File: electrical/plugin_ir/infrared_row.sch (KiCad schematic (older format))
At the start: 17 parts, among them U2 QRE1113GR, U3 QRE1113GR, U4 QRE1113GR, U5 QRE1113GR, U6 QRE1113GR, U7 QRE1113GR, U8 QRE1113GR, U9 CD4051B

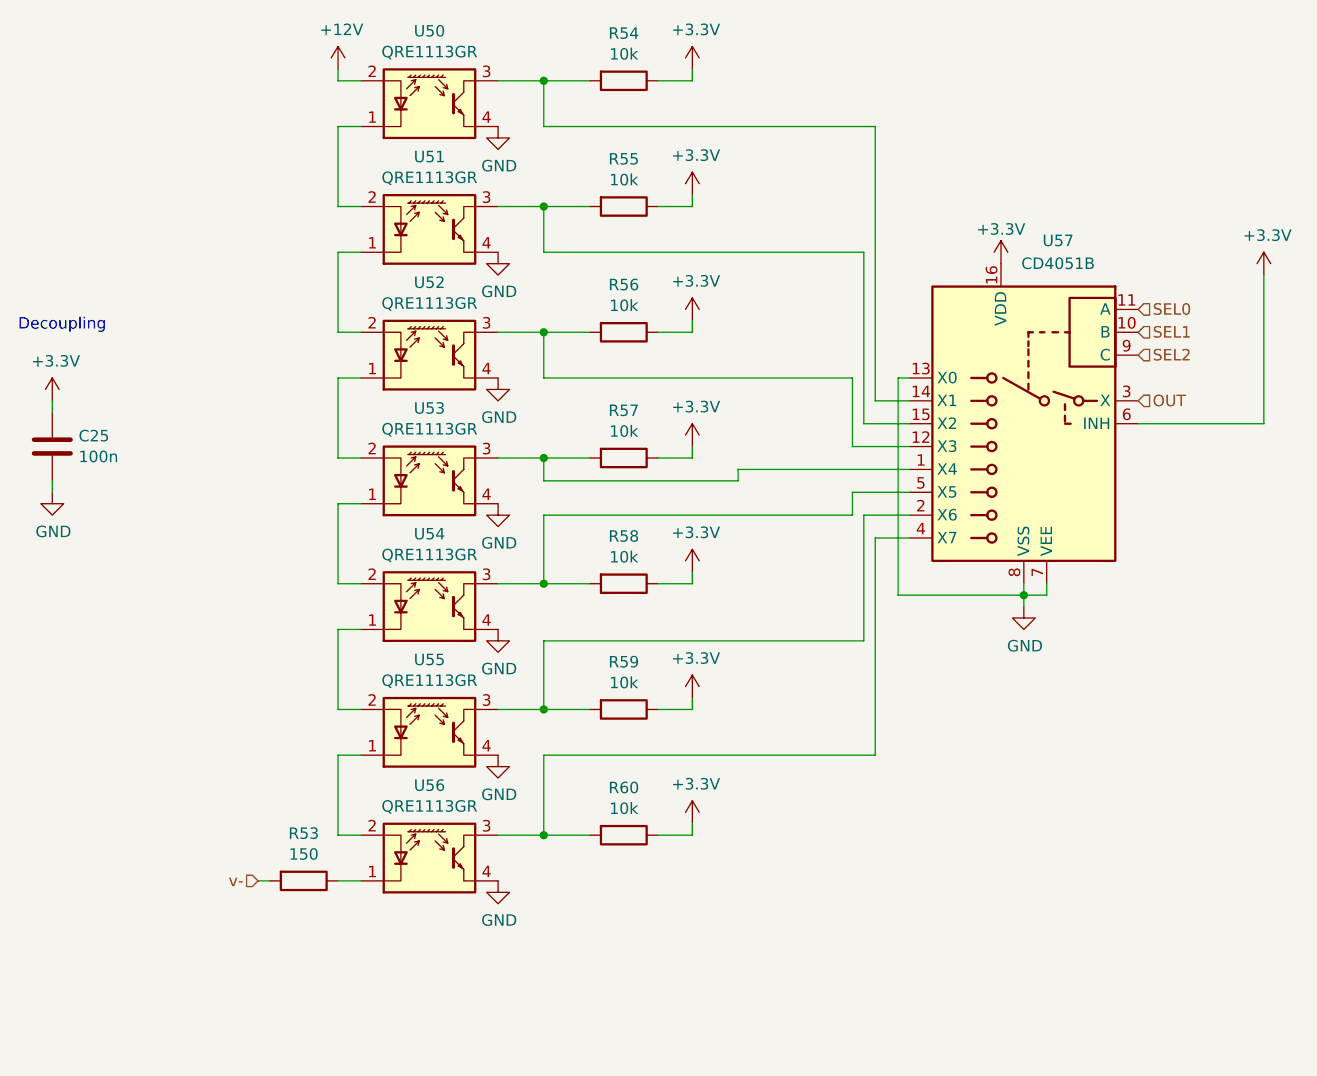
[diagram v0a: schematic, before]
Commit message: Project divided into Core and Plugins
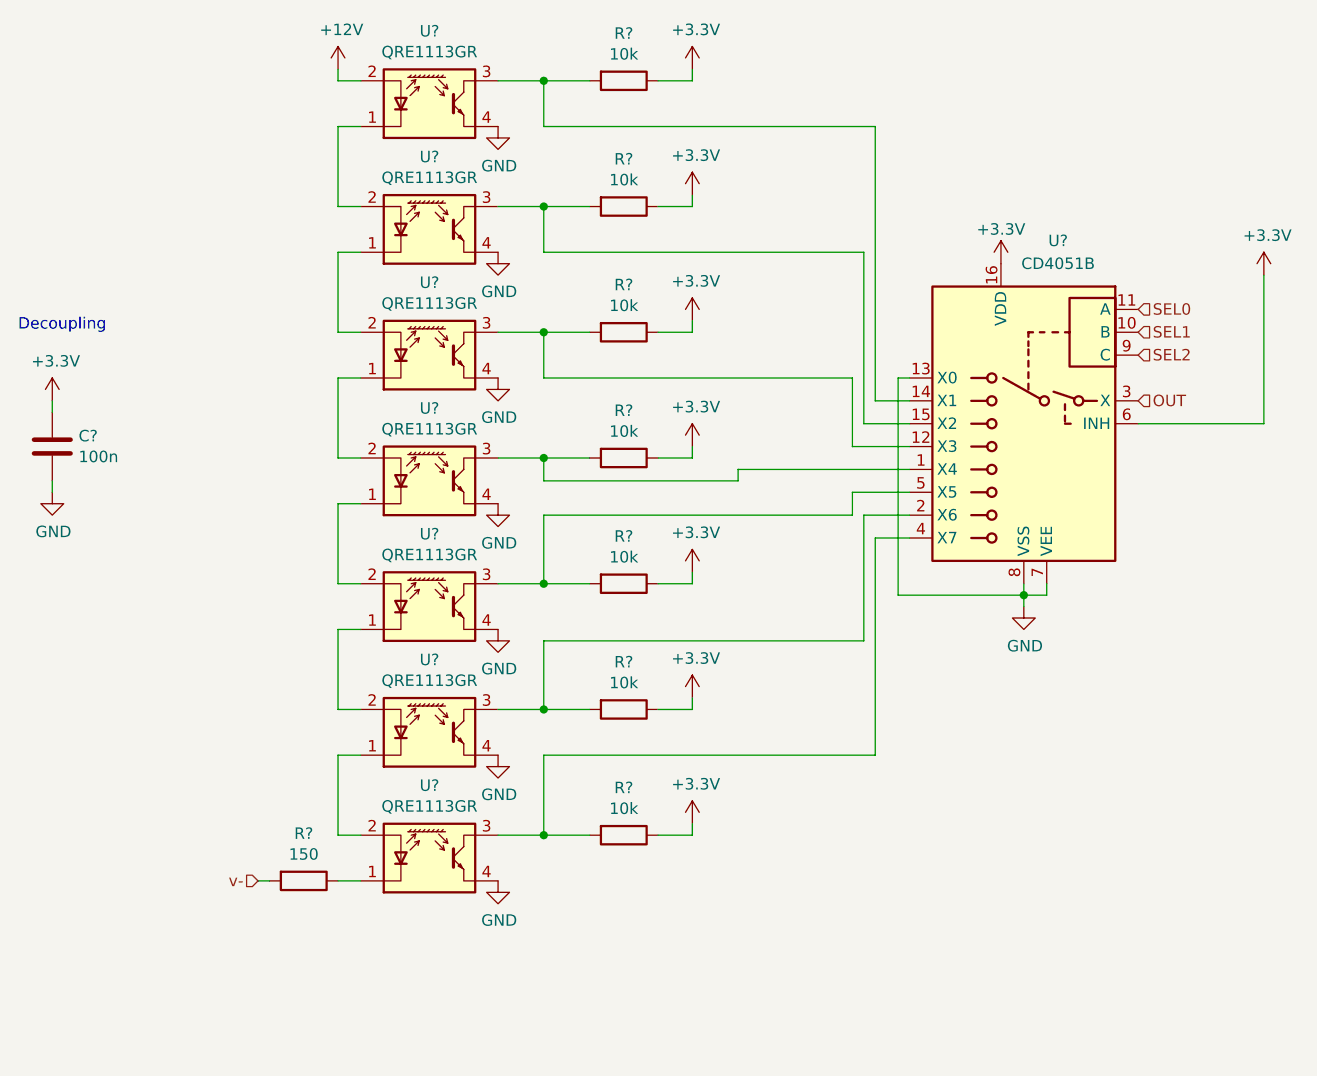
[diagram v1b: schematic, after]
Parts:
- renumbered C19 to C?, R6 to R?, R7 to R?, R8 to R?, R9 to R?, R10 to R?, R11 to R?, R12 to R?, R53 to R?, U9 to U?, U7 to U?, U6 to U?, U5 to U?, U4 to U?, U3 to U?, U2 to U?, U8 to U?

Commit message: Give Up SEPIC and 9V LDO design
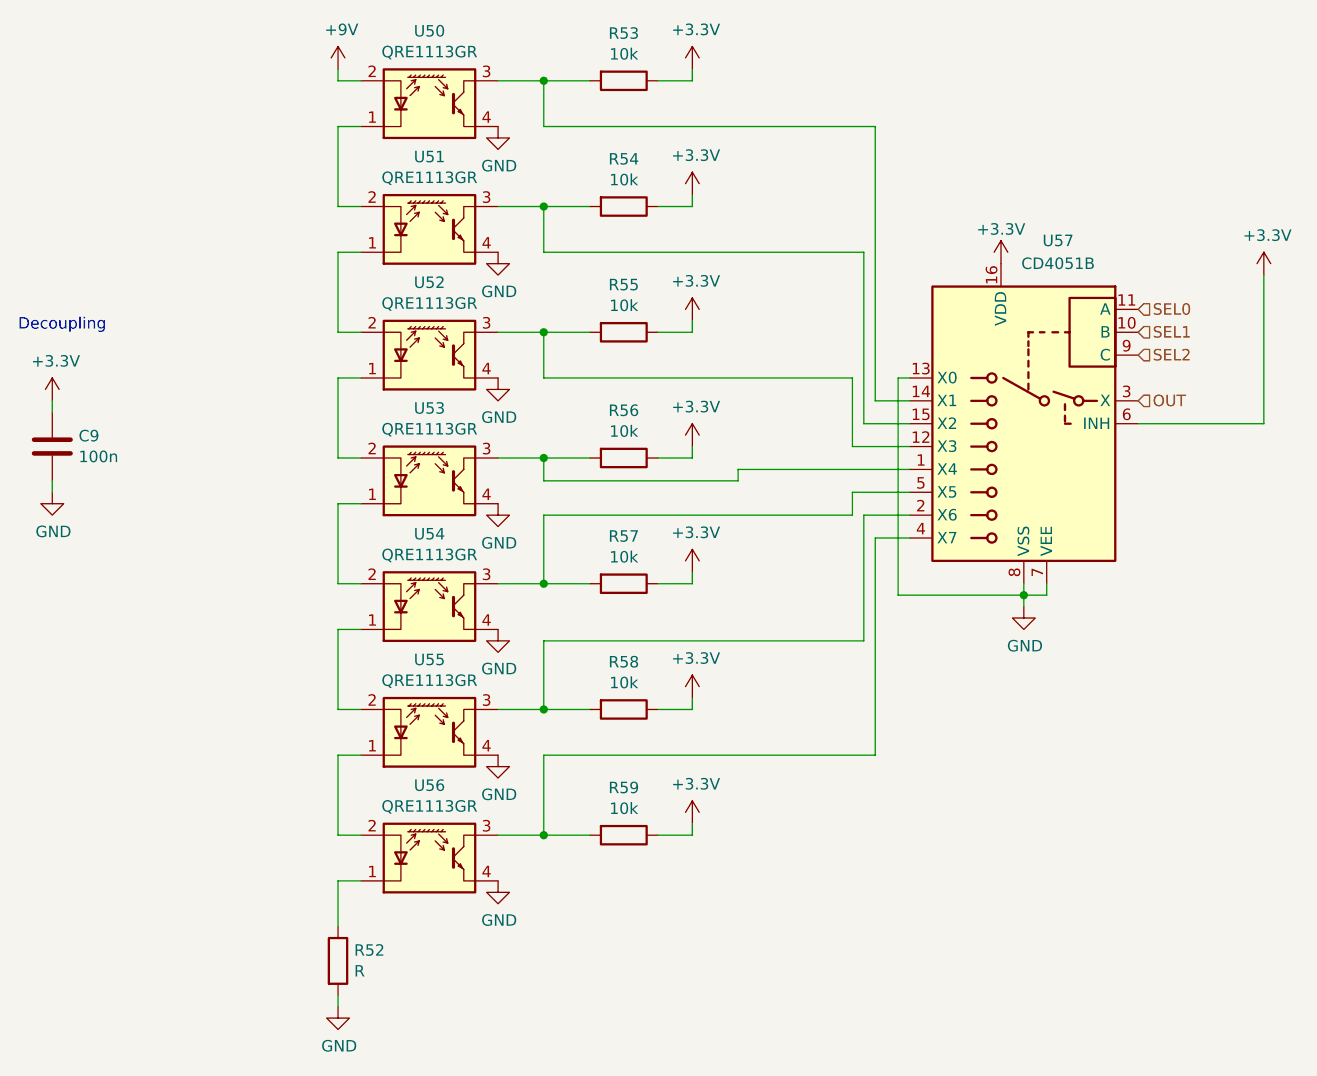
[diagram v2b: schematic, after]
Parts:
- removed R?: 150, Resistor_SMD:R_0805_2012Metric, symbol Device:R
- added R52: R, symbol Device:R
- gave numbers to parts that had none: 16
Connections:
- net GND: now also R52.2
- net at U56.1 (K): now also R52.1
- net +12V renamed +9V
